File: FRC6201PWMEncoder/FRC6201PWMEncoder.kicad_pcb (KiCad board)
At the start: 2 copper layers, 38 x 22.5 mm, 20 parts, among them J1 Conn_01x05, J2 Conn_02x05_Odd_Even, U1 AS5047D

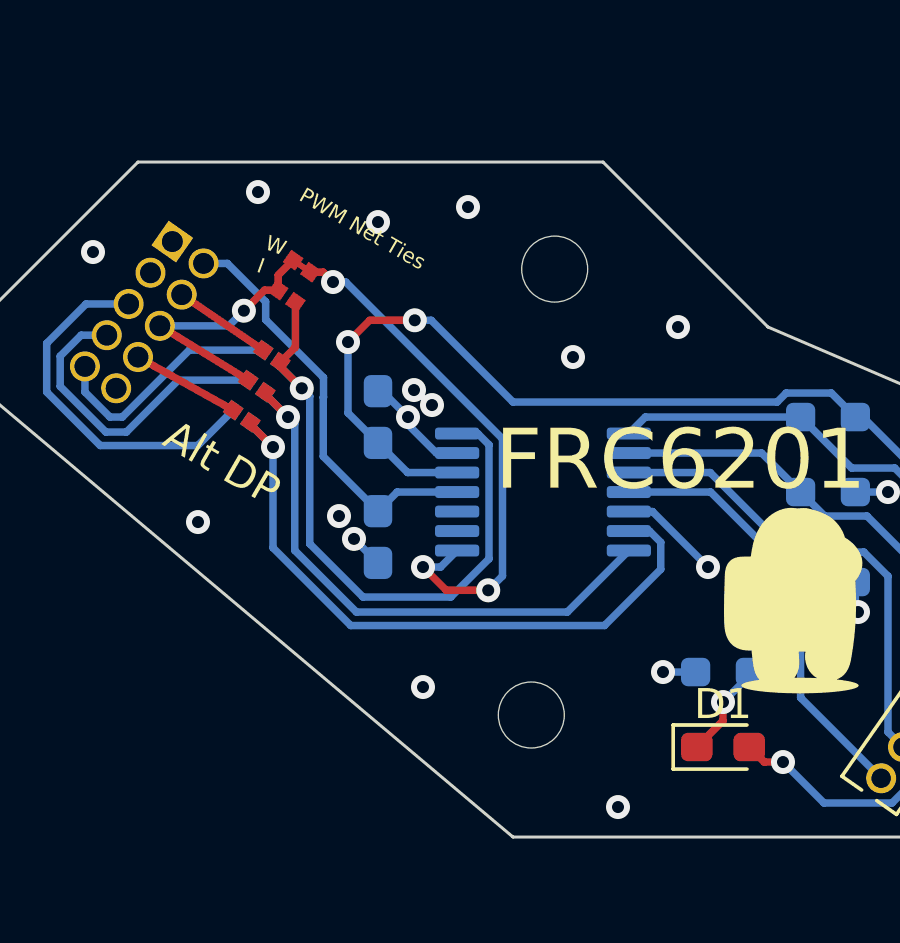
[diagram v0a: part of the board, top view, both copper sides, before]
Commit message: Increased Hole size to M3
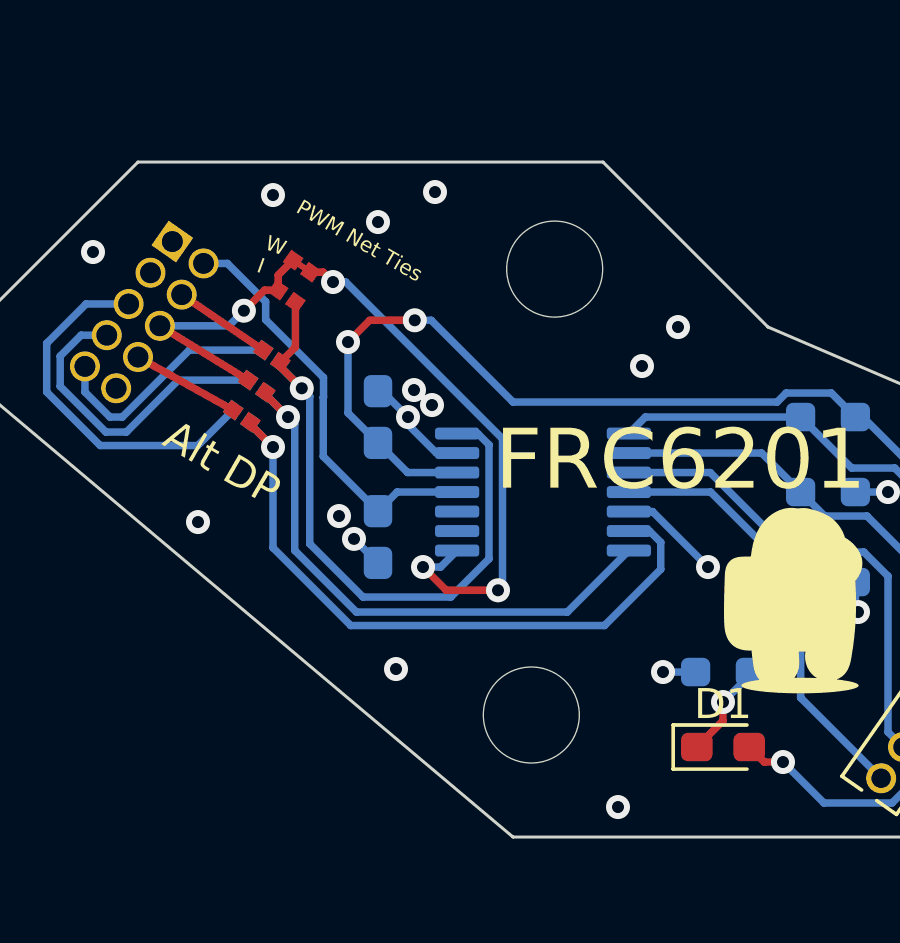
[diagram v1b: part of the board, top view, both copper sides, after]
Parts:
- removed H1, H2: MountingHole, MountingHole:MountingHole_2.2mm_M2
- added REF**: MountingHole_3.2mm_M3, MountingHole:MountingHole_3.2mm_M3, F.Cu at (-0.39, 7.43)
- added REF**: MountingHole_3.2mm_M3, MountingHole:MountingHole_3.2mm_M3, F.Cu at (0.39, -7.43)
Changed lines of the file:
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@@
       (net 13 "/a_alt") (pinfunction "2") (pintype "passive"))
+  )
+  (footprint "MountingHole:MountingHole_3.2mm_M3" (layer "F.Cu")
+    (at -0.389496 7.432001)
+    (descr "Mounting Hole 3.2mm, no annular, M3")
+    (tags "mounting hole 3.2mm no annular m3")
+    (attr exclude_from_pos_files exclude_from_bom)
+    (fp_text reference "REF**" (at 0 -4.2) (layer "F.SilkS") hide
+        (effects (font (size 1 1) (thickness 0.15)))
+    )
+    (fp_text value "MountingHole_3.2mm_M3" (at 0 4.2) (layer "F.Fab")
+        (effects (font (size 1 1) (thickness 0.15)))
+    )
+    (fp_text user "${REFERENCE}" (at 0 0) (layer "F.Fab")
+        (effects (font (size 1 1) (thickness 0.15)))
+    )
+    (fp_circle (center 0 0) (end 3.2 0)
+      (stroke (width 0.15) (type solid)) (fill none) (layer "Cmts.User"))
+    (fp_circle (center 0 0) (end 3.45 0)
+      (stroke (width 0.05) (type solid)) (fill none) (layer "F.CrtYd"))
+    (pad "" np_thru_hole circle (at 0 0) (size 3.2 3.2) (drill 3.2) (layers "*.Cu" "*.Mask"))
   )
   (footprint "Library:Jumper" (layer "F.Cu")
@@
       (net 13 "/a_alt") (pinfunction "2") (pintype "passive"))
   )
-  (footprint "MountingHole:MountingHole_2.2mm_M2" locked (layer "F.Cu")
-    (at -0.389496 7.432001 -80)
-    (descr "Mounting Hole 2.2mm, no annular, M2")
-    (tags "mounting hole 2.2mm no annular m2")
-    (property "Sheetfile" "THE_ENCODER.kicad_sch")
-    (property "Sheetname" "")
-    (property "ki_description" "Mounting Hole without connection")
-    (property "ki_keywords" "mounting hole")
-    (attr exclude_from_pos_files)
-    (fp_text reference "H2" (at 0 -3.2 100) (layer "F.SilkS") hide
+  (footprint "MountingHole:MountingHole_3.2mm_M3" (layer "F.Cu")
+    (at 0.389496 -7.432001)
+    (descr "Mounting Hole 3.2mm, no annular, M3")
+    (tags "mounting hole 3.2mm no annular m3")
+    (attr exclude_from_pos_files exclude_from_bom)
+    (fp_text reference "REF**" (at -0.789496 -2.467999) (layer "F.SilkS") hide
         (effects (font (size 1 1) (thickness 0.15)))
     )
-    (fp_text value "MountingHole" (at 0 3.2 100) (layer "F.Fab")
+    (fp_text value "MountingHole_3.2mm_M3" (at 0 4.2) (layer "F.Fab")
         (effects (font (size 1 1) (thickness 0.15)))
     )
-    (fp_text user "${REFERENCE}" (at 0 0 100) (layer "F.Fab")
+    (fp_text user "${REFERENCE}" (at 0 0) (layer "F.Fab")
         (effects (font (size 1 1) (thickness 0.15)))
     )
-    (fp_circle (center 0 0) (end 2.2 0)
+    (fp_circle (center 0 0) (end 3.2 0)
       (stroke (width 0.15) (type solid)) (fill none) (layer "Cmts.User"))
-    (fp_circle (center 0 0) (end 2.45 0)
+    (fp_circle (center 0 0) (end 3.45 0)
       (stroke (width 0.05) (type solid)) (fill none) (layer "F.CrtYd"))
-    (pad "" np_thru_hole circle locked (at 0 0 280) (size 2.2 2.2) (drill 2.2) (layers "*.Cu" "*.Mask"))
-  )
-  (footprint "MountingHole:MountingHole_2.2mm_M2" locked (layer "F.Cu")
-    (at 0.389496 -7.432001 -80)
-    (descr "Mounting Hole 2.2mm, no annular, M2")
-    (tags "mounting hole 2.2mm no annular m2")
-    (property "Sheetfile" "THE_ENCODER.kicad_sch")
-    (property "Sheetname" "")
-    (property "ki_description" "Mounting Hole without connection")
-    (property "ki_keywords" "mounting hole")
-    (attr exclude_from_pos_files)
-    (fp_text reference "H1" (at 0 -3.2 100) (layer "F.SilkS") hide
-        (effects (font (size 1 1) (thickness 0.15)))
-    )
-    (fp_text value "MountingHole" (at 0 3.2 100) (layer "F.Fab")
-        (effects (font (size 1 1) (thickness 0.15)))
-    )
-    (fp_text user "${REFERENCE}" (at 0 0 100) (layer "F.Fab")
-        (effects (font (size 1 1) (thickness 0.15)))
-    )
-    (fp_circle (center 0 0) (end 2.2 0)
-      (stroke (width 0.15) (type solid)) (fill none) (layer "Cmts.User"))
-    (fp_circle (center 0 0) (end 2.45 0)
-      (stroke (width 0.05) (type solid)) (fill none) (layer "F.CrtYd"))
-    (pad "" np_thru_hole circle locked (at 0 0 280) (size 2.2 2.2) (drill 2.2) (layers "*.Cu" "*.Mask"))
+    (pad "" np_thru_hole circle (at 0 0) (size 3.2 3.2) (drill 3.2) (layers "F&B.Cu" "*.Mask"))
   )
   (footprint "Capacitor_SMD:C_0603_1608Metric_Pad1.08x0.95mm_HandSolder" (layer "B.Cu")
@@
     (effects (font (size 2 2) (thickness 0.3)) (justify left bottom))
   )
-  (gr_text "PWM Net Ties" (at -8.2 -9.7 330) (layer "F.SilkS")
+  (gr_text "PWM Net Ties" (at -8.3 -9.3 330) (layer "F.SilkS")
     (effects (font (size 0.5 0.5) (thickness 0.125)) (justify left bottom))
   )
@@
   (via (at -18.5 -5) (size 0.8) (drill 0.4) (layers "F.Cu" "B.Cu") (free) (net 1))
   (via (at -6.3 1.5625) (size 0.8) (drill 0.4) (layers "F.Cu" "B.Cu") (net 1))
-  (via (at -4 6.5) (size 0.8) (drill 0.4) (layers "F.Cu" "B.Cu") (free) (net 1))
+  (via (at -4.9 5.9) (size 0.8) (drill 0.4) (layers "F.Cu" "B.Cu") (free) (net 1))
   (via (at 5.5 2.5) (size 0.8) (drill 0.4) (layers "F.Cu" "B.Cu") (free) (net 1))
   (via (at -3.7 -2.9) (size 0.8) (drill 0.4) (layers "F.Cu" "B.Cu") (free) (net 1))
-  (via (at 1 -4.5) (size 0.8) (drill 0.4) (layers "F.Cu" "B.Cu") (free) (net 1))
+  (via (at 3.3 -4.2) (size 0.8) (drill 0.4) (layers "F.Cu" "B.Cu") (free) (net 1))
   (via (at -4.3 -3.4) (size 0.8) (drill 0.4) (layers "F.Cu" "B.Cu") (free) (net 1))
   (via (at -11.5 1) (size 0.8) (drill 0.4) (layers "F.Cu" "B.Cu") (free) (net 1))
-  (via (at -2.5 -9.5) (size 0.8) (drill 0.4) (layers "F.Cu" "B.Cu") (free) (net 1))
-  (via (at -9.5 -10) (size 0.8) (drill 0.4) (layers "F.Cu" "B.Cu") (free) (net 1))
+  (via (at -3.6 -10) (size 0.8) (drill 0.4) (layers "F.Cu" "B.Cu") (free) (net 1))
+  (via (at -9 -9.9) (size 0.8) (drill 0.4) (layers "F.Cu" "B.Cu") (free) (net 1))
   (via (at 4.5 -5.5) (size 0.8) (drill 0.4) (layers "F.Cu" "B.Cu") (free) (net 1))
   (via (at 11.5 0) (size 0.8) (drill 0.4) (layers "F.Cu" "B.Cu") (net 1))
@@
   (segment (start 11.500001 2.804506) (end 10.695495 2) (width 0.25) (layer "B.Cu") (net 7))
   (segment (start -7.327927 -7.327927) (end -7 -7) (width 0.25) (layer "F.Cu") (net 8))
-  (segment (start -1.825545 3.2755) (end -3.2245 3.2755) (width 0.25) (layer "F.Cu") (net 8))
   (segment (start -3.2245 3.2755) (end -4 2.5) (width 0.25) (layer "F.Cu") (net 8))
+  (segment (start -1.5 3.2755) (end -3.2245 3.2755) (width 0.25) (layer "F.Cu") (net 8))
   (segment (start -7.754254 -7.327927) (end -7.327927 -7.327927) (width 0.25) (layer "F.Cu") (net 8))
   (via (at -4 2.5) (size 0.8) (drill 0.4) (layers "F.Cu" "B.Cu") (net 8))
   (via (at -7 -7) (size 0.8) (drill 0.4) (layers "F.Cu" "B.Cu") (net 8))
-  (via (at -1.825545 3.2755) (size 0.8) (drill 0.4) (layers "F.Cu" "B.Cu") (net 8))
+  (via (at -1.5 3.2755) (size 0.8) (drill 0.4) (layers "F.Cu" "B.Cu") (net 8))
+  (segment (start -1.35 -1.776041) (end -6.573959 -7) (width 0.25) (layer "B.Cu") (net 8))
+  (segment (start -6.573959 -7) (end -7 -7) (width 0.25) (layer "B.Cu") (net 8))
   (segment (start -4 2.5) (end -3.4125 2.5) (width 0.25) (layer "B.Cu") (net 8))
-  (segment (start -1.35 2.799955) (end -1.825545 3.2755) (width 0.25) (layer "B.Cu") (net 8))
-  (segment (start -7 -7) (end -6.573959 -7) (width 0.25) (layer "B.Cu") (net 8))
   (segment (start -3.4125 2.5) (end -2.8625 1.95) (width 0.25) (layer "B.Cu") (net 8))
-  (segment (start -1.35 -1.776041) (end -1.35 2.799955) (width 0.25) (layer "B.Cu") (net 8))
-  (segment (start -6.573959 -7) (end -1.35 -1.776041) (width 0.25) (layer "B.Cu") (net 8))
+  (segment (start -1.5 3.2755) (end -1.35 3.1255) (width 0.25) (layer "B.Cu") (net 8))
+  (segment (start -1.35 3.1255) (end -1.35 -1.776041) (width 0.25) (layer "B.Cu") (net 8))
   (segment (start -5.77468 -5.72532) (end -6.5 -5) (width 0.25) (layer "F.Cu") (net 9))
   (segment (start 7.375 9) (end 6.875 8.5) (width 0.25) (layer "F.Cu") (net 9))
